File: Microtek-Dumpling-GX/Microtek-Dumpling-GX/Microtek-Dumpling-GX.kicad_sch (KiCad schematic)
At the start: 20 parts, among them P1 AppleIIBus, P2 Conn_02x13, U1 74LS02, U2 74LS86, U3 74LS133, U4 74LS244, U5 74LS273, U6 27C32, U7 74LS08, U8 74LS279, U9 74LS138

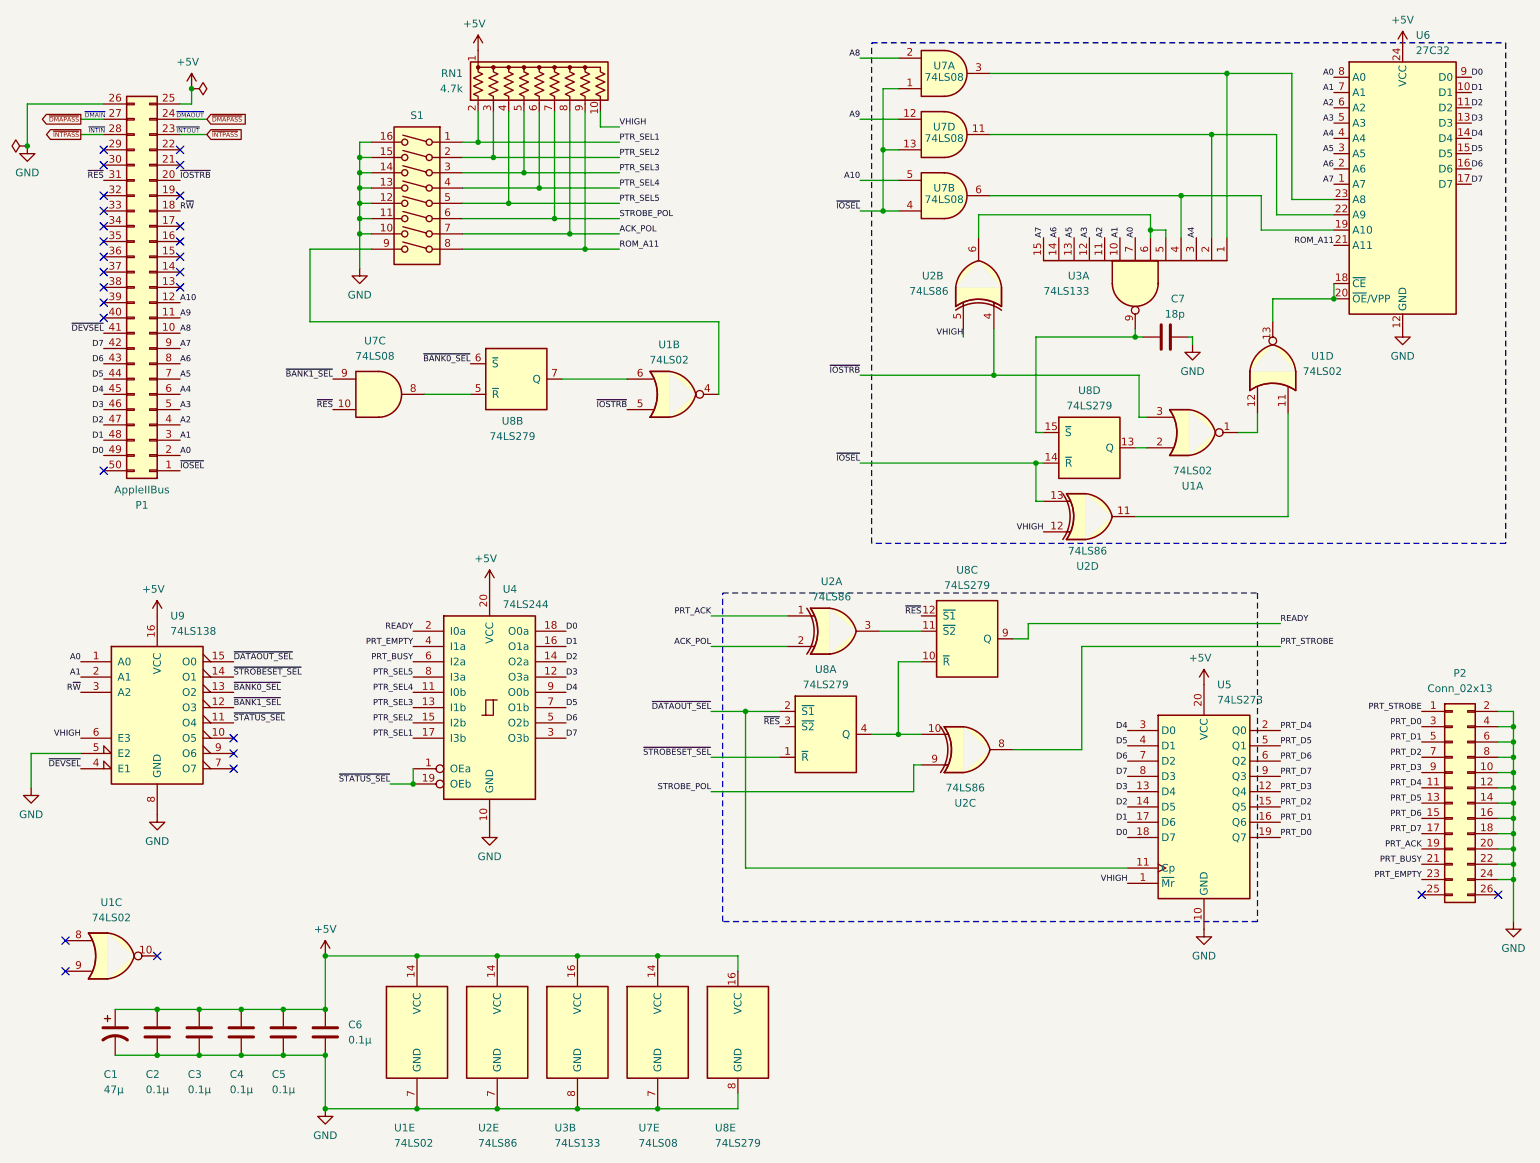
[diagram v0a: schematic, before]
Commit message: Update the Dumpling-GX project to kicad8 and the shared symbol library
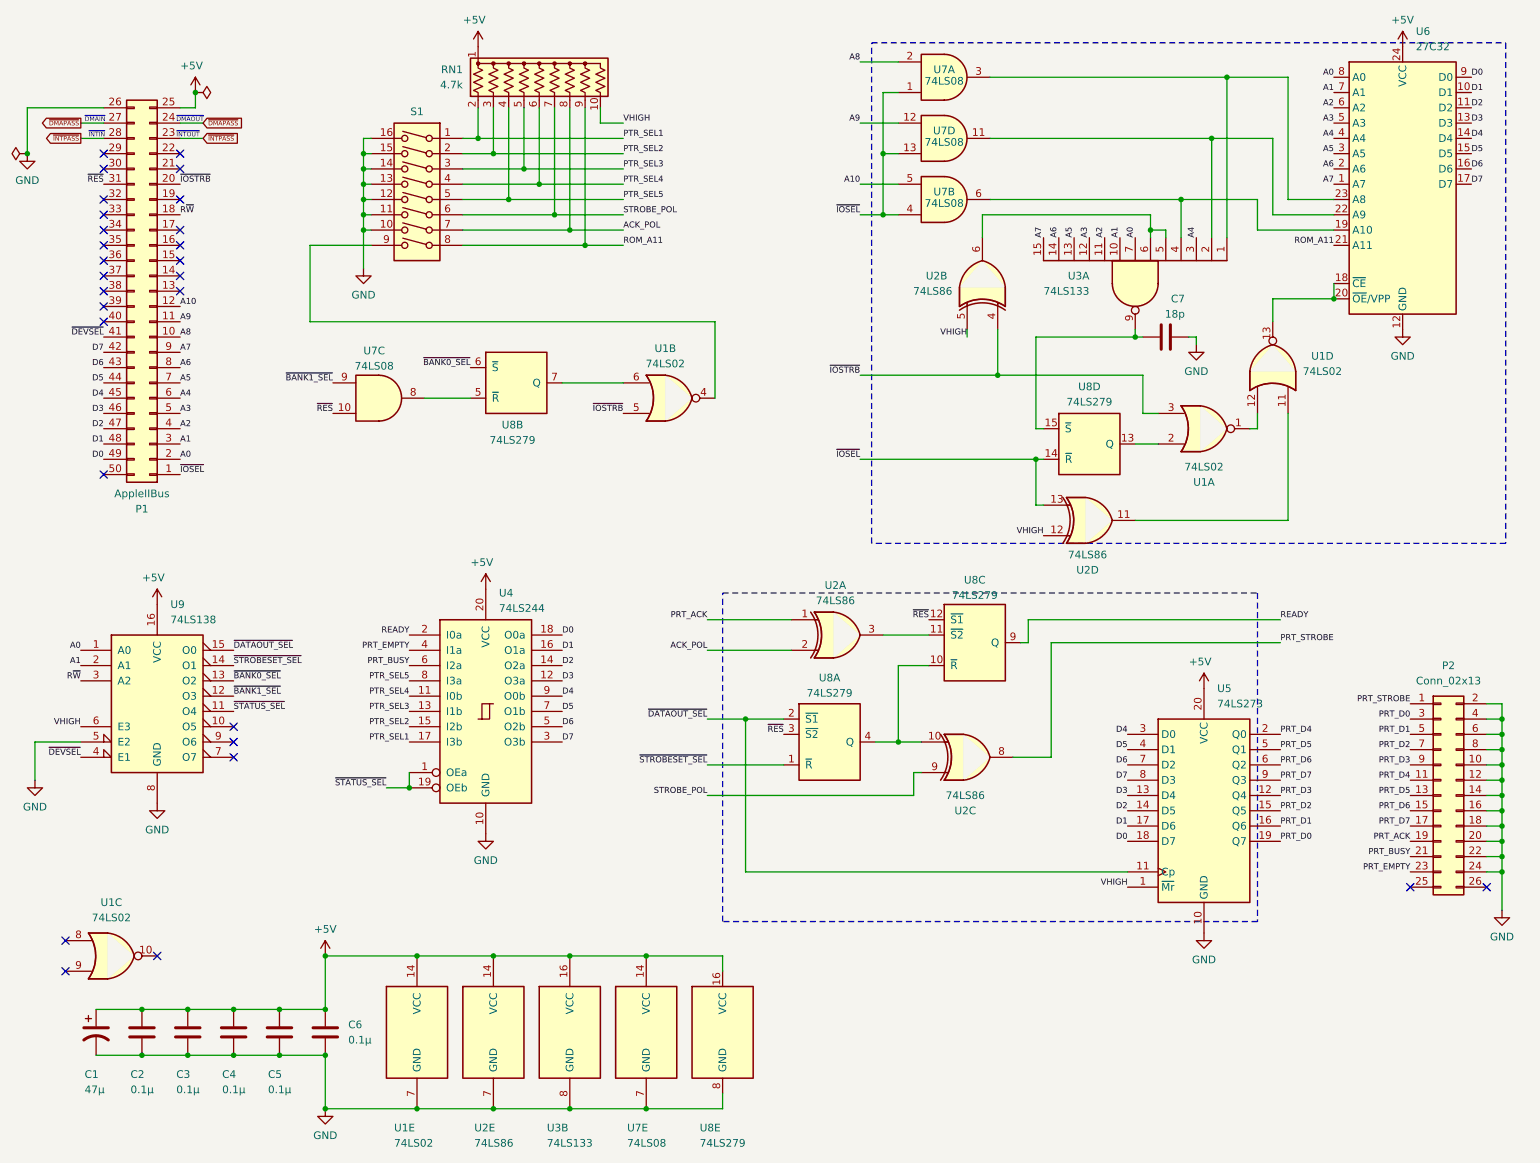
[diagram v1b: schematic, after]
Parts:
- P1: footprint Apple:AppleIIBus_Edge -> (none)
- U6: symbol Memory:27C32 -> Memory_Legacy:27C32
- U8: symbol Logic:74LS279 -> Logic_Legacy:74LS279
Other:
- moved on the sheet: C1, C2, C3, C4, C5, P1, P2, RN1, S1, U1A, U1B, U2A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
